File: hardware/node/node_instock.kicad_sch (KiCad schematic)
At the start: 53 parts, among them IC1 MCP73844-840I_MS, IC2 NEO-M9N-00B, J1 USB_C_Receptacle, J2 OMEGA2_HEADER, Q1 IRF7404, Q2 AO3400A, Q3 S8550, SW1 SW_POWER, U3 ADS1115IDGS, U4 Omega2S

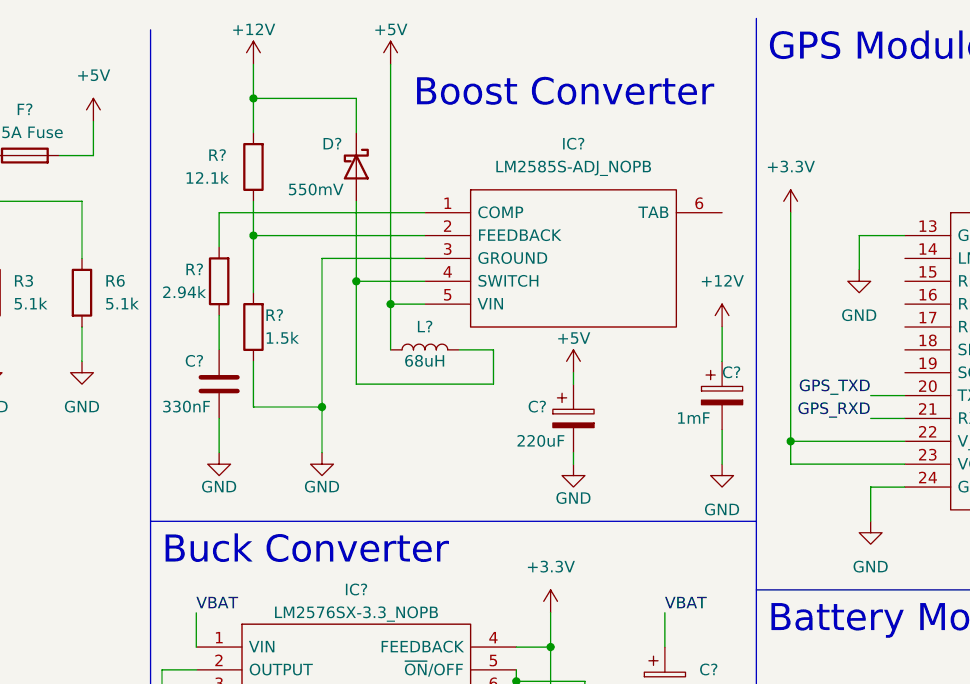
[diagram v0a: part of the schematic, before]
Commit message: update boost converter
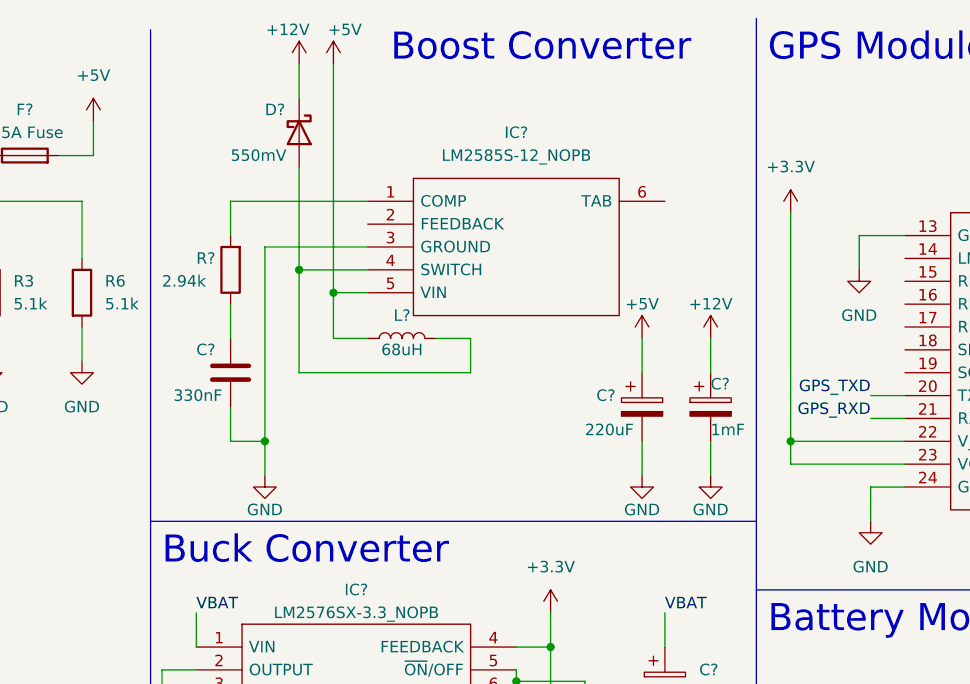
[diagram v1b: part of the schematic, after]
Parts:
- removed IC?: LM2585S-ADJ_NOPB, TO170P1435X465-6N, symbol Boost_Converter:LM2585S-ADJ_NOPB
- removed R?: 12.1k, symbol Device:R
- removed R?: 1.5k, symbol Device:R
- added IC?: LM2585S-12_NOPB, TO170P1435X465-6N, symbol Boost_Converter_12v:LM2585S-12_NOPB
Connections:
- net +5V: now also IC?.5 (VIN)
- net GND: now also IC?.3 (GROUND)
- net at D?.2 (A), L?.2: now also IC?.4 (SWITCH)
- net at R?.2: now also IC?.1 (COMP)
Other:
- moved on the sheet: C?, D?, L?, R?

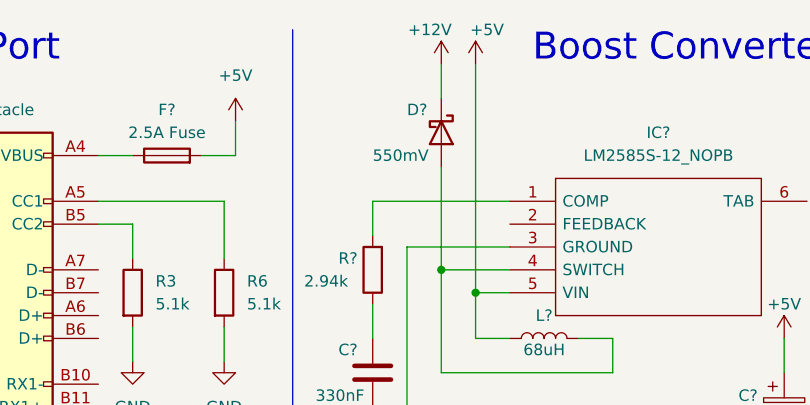
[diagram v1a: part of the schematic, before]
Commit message: fix missing connection in boost converter
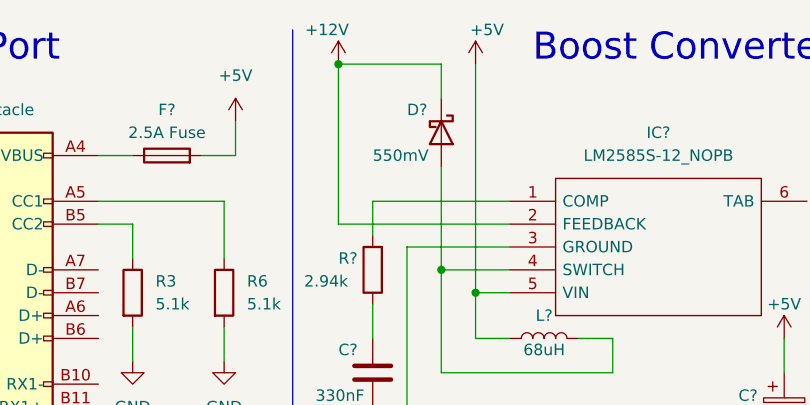
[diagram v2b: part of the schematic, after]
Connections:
- net +12V: now also IC?.2 (FEEDBACK)
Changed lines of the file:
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@@
   (junction (at 140.97 109.22) (diameter 0) (color 0 0 0 0)
   )
+  (junction (at 66.04 17.78) (diameter 0) (color 0 0 0 0)
+  )
   (junction (at 49.53 147.32) (diameter 0) (color 0 0 0 0)
   )
@@
     (stroke (width 0) (type default) (color 0 0 0 0))
   )
+  (wire (pts (xy 66.04 35.56) (xy 66.04 17.78))
+    (stroke (width 0) (type default) (color 0 0 0 0))
+  )
   (wire (pts (xy 106.68 186.69) (xy 102.87 186.69))
     (stroke (width 0) (type default) (color 0 0 0 0))
@@
     (stroke (width 0) (type default) (color 0 0 0 0))
   )
+  (wire (pts (xy 85.09 35.56) (xy 66.04 35.56))
+    (stroke (width 0) (type default) (color 0 0 0 0))
+  )
   (wire (pts (xy 193.04 36.83) (xy 196.85 36.83))
     (stroke (width 0) (type default) (color 0 0 0 0))
@@
   )
   (wire (pts (xy 115.57 48.26) (xy 115.57 52.07))
+    (stroke (width 0) (type default) (color 0 0 0 0))
+  )
+  (wire (pts (xy 66.04 17.78) (xy 77.47 17.78))
     (stroke (width 0) (type default) (color 0 0 0 0))
   )
@@
     (pin "1")
   )
-  (symbol (lib_id "power:+12V") (at 77.47 17.78 0) (unit 1)
+  (symbol (lib_id "power:+12V") (at 66.04 17.78 0) (unit 1)
     (in_bom yes) (on_board yes)
-    (property "Reference" "#PWR?" (id 0) (at 77.47 21.59 0)
-      (effects (font (size 1.27 1.27)) hide)
-    )
-    (property "Value" "+12V" (id 1) (at 76.2 13.97 0))
-    (property "Footprint" "" (id 2) (at 77.47 17.78 0)
-      (effects (font (size 1.27 1.27)) hide)
-    )
-    (property "Datasheet" "" (id 3) (at 77.47 17.78 0)
-      (effects (font (size 1.27 1.27)) hide)
-    )
+    (property "Reference" "#PWR?" (id 0) (at 66.04 21.59 0)
+      (effects (font (size 1.27 1.27)) hide)
+    )
+    (property "Value" "+12V" (id 1) (at 64.77 13.97 0))
+    (property "Footprint" "" (id 2) (at 66.04 17.78 0)
+      (effects (font (size 1.27 1.27)) hide)
+    )
+    (property "Datasheet" "" (id 3) (at 66.04 17.78 0)
+      (effects (font (size 1.27 1.27)) hide)
+    )
